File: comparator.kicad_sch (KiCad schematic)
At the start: 5 parts

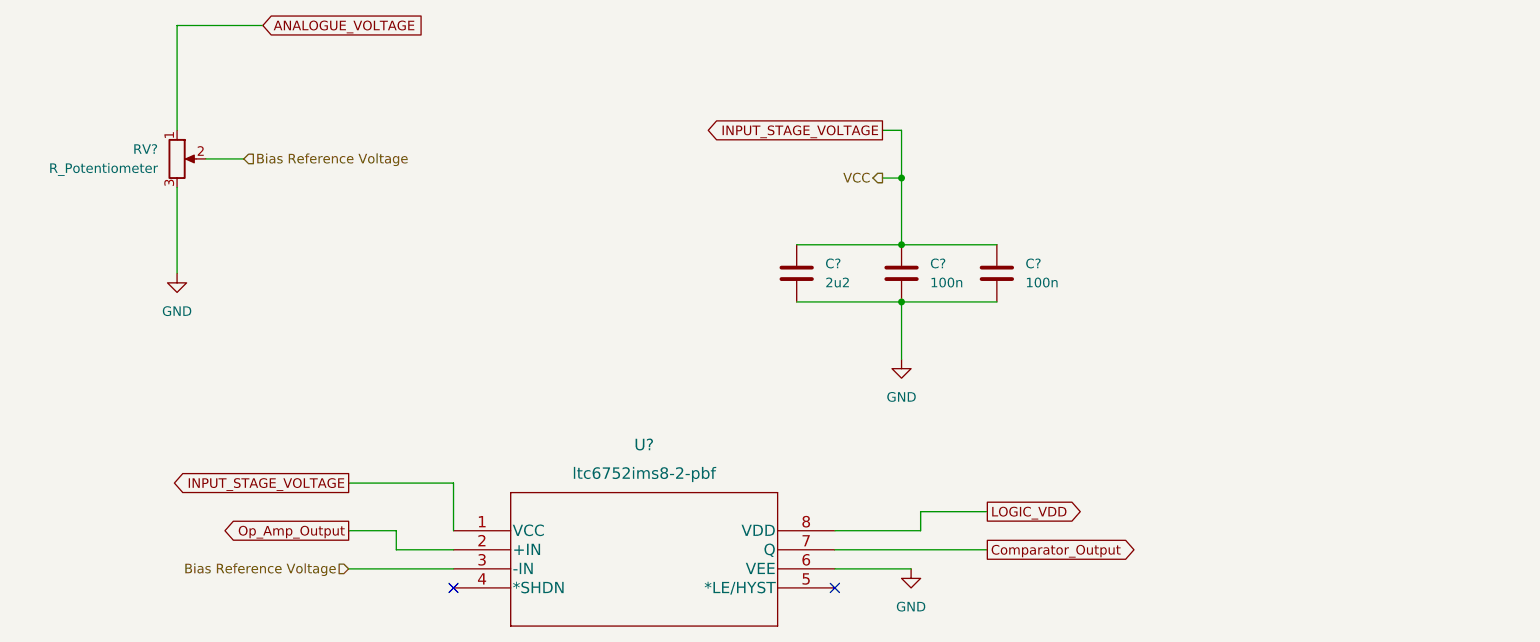
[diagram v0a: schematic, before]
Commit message: add comparator caps
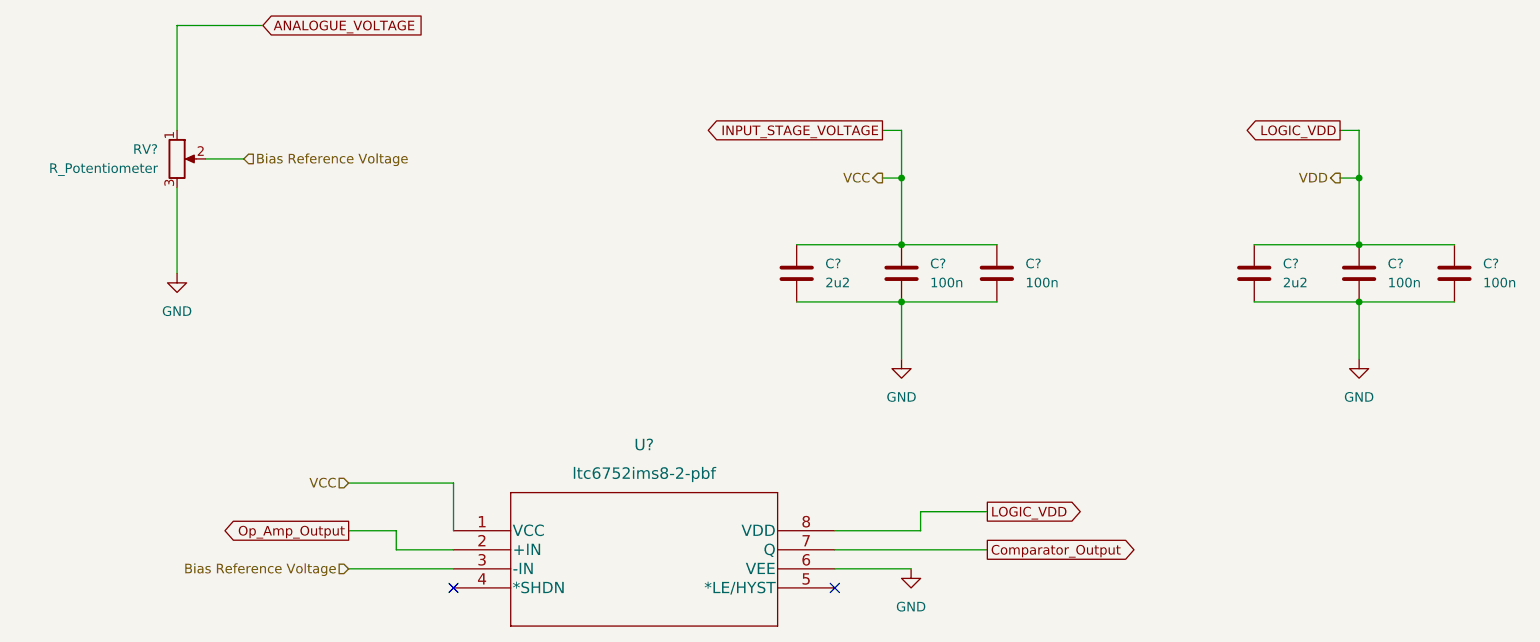
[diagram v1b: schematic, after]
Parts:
- added C? (x2): 100n, symbol Device:C
- added C?: 2u2, symbol Device:C
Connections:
- net GND: now also C?.2, C?.2, C?.2
- net LOGIC_VDD: now also C?.1, C?.1, C?.1
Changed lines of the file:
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@@
   (junction (at 172.72 44.45) (diameter 0) (color 0 0 0 0)
   )
+  (junction (at 233.68 53.34) (diameter 0) (color 0 0 0 0)
+  )
+  (junction (at 233.68 60.96) (diameter 0) (color 0 0 0 0)
+  )
   (junction (at 172.72 60.96) (diameter 0) (color 0 0 0 0)
+  )
+  (junction (at 233.68 44.45) (diameter 0) (color 0 0 0 0)
   )
   (no_connect (at 113.03 99.06))
   (no_connect (at 163.83 99.06))
+  (wire (pts (xy 233.68 60.96) (xy 246.38 60.96))
+    (stroke (width 0) (type default) (color 0 0 0 0))
+  )
   (wire (pts (xy 172.72 44.45) (xy 172.72 53.34))
     (stroke (width 0) (type default) (color 0 0 0 0))
@@
     (stroke (width 0) (type default) (color 0 0 0 0))
   )
+  (wire (pts (xy 233.68 60.96) (xy 233.68 68.58))
+    (stroke (width 0) (type default) (color 0 0 0 0))
+  )
   (wire (pts (xy 170.18 44.45) (xy 172.72 44.45))
     (stroke (width 0) (type default) (color 0 0 0 0))
@@
     (stroke (width 0) (type default) (color 0 0 0 0))
   )
+  (wire (pts (xy 231.14 38.1) (xy 233.68 38.1))
+    (stroke (width 0) (type default) (color 0 0 0 0))
+  )
   (wire (pts (xy 163.83 96.52) (xy 173.99 96.52))
     (stroke (width 0) (type default) (color 0 0 0 0))
@@
     (stroke (width 0) (type default) (color 0 0 0 0))
   )
+  (wire (pts (xy 233.68 38.1) (xy 233.68 44.45))
+    (stroke (width 0) (type default) (color 0 0 0 0))
+  )
+  (wire (pts (xy 219.71 60.96) (xy 233.68 60.96))
+    (stroke (width 0) (type default) (color 0 0 0 0))
+  )
   (wire (pts (xy 172.72 60.96) (xy 172.72 68.58))
     (stroke (width 0) (type default) (color 0 0 0 0))
@@
     (stroke (width 0) (type default) (color 0 0 0 0))
   )
+  (wire (pts (xy 233.68 44.45) (xy 233.68 53.34))
+    (stroke (width 0) (type default) (color 0 0 0 0))
+  )
   (wire (pts (xy 105.41 93.98) (xy 105.41 91.44))
     (stroke (width 0) (type default) (color 0 0 0 0))
@@
     (stroke (width 0) (type default) (color 0 0 0 0))
   )
+  (wire (pts (xy 231.14 44.45) (xy 233.68 44.45))
+    (stroke (width 0) (type default) (color 0 0 0 0))
+  )
+  (wire (pts (xy 233.68 53.34) (xy 246.38 53.34))
+    (stroke (width 0) (type default) (color 0 0 0 0))
+  )
   (wire (pts (xy 158.75 60.96) (xy 172.72 60.96))
+    (stroke (width 0) (type default) (color 0 0 0 0))
+  )
+  (wire (pts (xy 219.71 53.34) (xy 233.68 53.34))
     (stroke (width 0) (type default) (color 0 0 0 0))
   )
@@
     (effects (font (size 1.27 1.27)) (justify right))
     (property "Intersheet References" "${INTERSHEET_REFS}" (id 0) (at 146.7212 38.0206 0)
-      (effects (font (size 1.27 1.27)) (justify right) hide)
-    )
-  )
-  (global_label "INPUT_STAGE_VOLTAGE" (shape output) (at 99.06 85.09 180) (fields_autoplaced)
-    (effects (font (size 1.27 1.27)) (justify right))
-    (property "Intersheet References" "${INTERSHEET_REFS}" (id 0) (at 75.6012 85.0106 0)
       (effects (font (size 1.27 1.27)) (justify right) hide)
     )
@@
     )
   )
+  (global_label "LOGIC_VDD" (shape output) (at 231.14 38.1 180) (fields_autoplaced)
+    (effects (font (size 1.27 1.27)) (justify right))
+    (property "Intersheet References" "${INTERSHEET_REFS}" (id 0) (at 218.6274 38.0206 0)
+      (effects (font (size 1.27 1.27)) (justify right) hide)
+    )
+  )
   (hierarchical_label "Bias Reference Voltage" (shape input) (at 99.06 96.52 180)
+    (effects (font (size 1.27 1.27)) (justify right))
+  )
+  (hierarchical_label "VCC" (shape input) (at 99.06 85.09 180)
     (effects (font (size 1.27 1.27)) (justify right))
   )
   (hierarchical_label "Bias Reference Voltage" (shape input) (at 85.09 41.91 0)
     (effects (font (size 1.27 1.27)) (justify left))
+  )
+  (hierarchical_label "VDD" (shape output) (at 231.14 44.45 180)
+    (effects (font (size 1.27 1.27)) (justify right))
   )
   (hierarchical_label "VCC" (shape output) (at 170.18 44.45 180)
@@
     (pin "2")
   )
+  (symbol (lib_id "Device:C") (at 233.68 57.15 0) (unit 1)
+    (in_bom yes) (on_board yes) (fields_autoplaced)
+    (property "Reference" "C?" (id 0) (at 237.49 55.8799 0)
+      (effects (font (size 1.27 1.27)) (justify left))
+    )
+    (property "Value" "100n" (id 1) (at 237.49 58.4199 0)
+      (effects (font (size 1.27 1.27)) (justify left))
+    )
+    (property "Footprint" "" (id 2) (at 234.6452 60.96 0)
+      (effects (font (size 1.27 1.27)) hide)
+    )
+    (property "Datasheet" "~" (id 3) (at 233.68 57.15 0)
+      (effects (font (size 1.27 1.27)) hide)
+    )
+    (pin "1")
+    (pin "2")
+  )
+  (symbol (lib_id "Device:C") (at 246.38 57.15 0) (unit 1)
+    (in_bom yes) (on_board yes) (fields_autoplaced)
+    (property "Reference" "C?" (id 0) (at 250.19 55.8799 0)
+      (effects (font (size 1.27 1.27)) (justify left))
+    )
+    (property "Value" "100n" (id 1) (at 250.19 58.4199 0)
+      (effects (font (size 1.27 1.27)) (justify left))
+    )
+    (property "Footprint" "" (id 2) (at 247.3452 60.96 0)
+      (effects (font (size 1.27 1.27)) hide)
+    )
+    (property "Datasheet" "~" (id 3) (at 246.38 57.15 0)
+      (effects (font (size 1.27 1.27)) hide)
+    )
+    (pin "1")
+    (pin "2")
+  )
+  (symbol (lib_id "power:GND") (at 233.68 68.58 0) (unit 1)
+    (in_bom yes) (on_board yes) (fields_autoplaced)
+    (property "Reference" "#PWR?" (id 0) (at 233.68 74.93 0)
+      (effects (font (size 1.27 1.27)) hide)
+    )
+    (property "Value" "GND" (id 1) (at 233.68 73.66 0))
+    (property "Footprint" "" (id 2) (at 233.68 68.58 0)
+      (effects (font (size 1.27 1.27)) hide)
+    )
+    (property "Datasheet" "" (id 3) (at 233.68 68.58 0)
+      (effects (font (size 1.27 1.27)) hide)
+    )
+    (pin "1")
+  )
   (symbol (lib_id "Device:C") (at 185.42 57.15 0) (unit 1)
     (in_bom yes) (on_board yes) (fields_autoplaced)
@@
       (effects (font (size 1.27 1.27)) hide)
     )
+    (pin "1")
+    (pin "2")
+  )
+  (symbol (lib_id "Device:C") (at 219.71 57.15 0) (unit 1)
+    (in_bom yes) (on_board yes) (fields_autoplaced)
+    (property "Reference" "C?" (id 0) (at 223.52 55.8799 0)
+      (effects (font (size 1.27 1.27)) (justify left))
+    )
+    (property "Value" "2u2" (id 1) (at 223.52 58.4199 0)
+      (effects (font (size 1.27 1.27)) (justify left))
+    )
+    (property "Footprint" "" (id 2) (at 220.6752 60.96 0)
+      (effects (font (size 1.27 1.27)) hide)
+    )
+    (property "Datasheet" "~" (id 3) (at 219.71 57.15 0)
+      (effects (font (size 1.27 1.27)) hide)
+    )
